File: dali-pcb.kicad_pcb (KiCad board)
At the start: 2 copper layers, 180.5 x 113 mm, 62 parts, among them J1 12-22.5V DC, J10 5V DC, J11 5V DC, J12 5V DC, J13 5V DC, J14 5V DC, J15 GND, J2 DALI BUS, J20 LOLIN-S3 (L), J21 LOLIN-S3 (R), J22 ESP32-S3-DEVKITC-1 (L), J23 ESP32-S3-DEVKITC-1 (R), J24 LOLIN-S3-MINI (L), J25 LOLIN-S3-MINI (R), J26 LOLIN-S2-MINI (L), J27 LOLIN-S2-MINI (R), J3 DALI BUS, J30 FTDI-MCU, J31 UART-DALI, J4 DALI BUS, J40 A10-0, J41 A5-0, J42 A5-5, J43 A2-0, J44 A2-2, J45 A2-4, J46 A2-6, J47 A2-8, J50 D8-11, J51 D4-11, J52 D4-16, J53 D2-11, J54 D2-13, J55 D2-16, J56 D2-18, J60 D1-11, J61 D1-12, J62 D1-13, J63 D1-14, Q1 PZT2222A, Q2 MMBT2222A, U1 TCLT1000, U2 TCLT1000

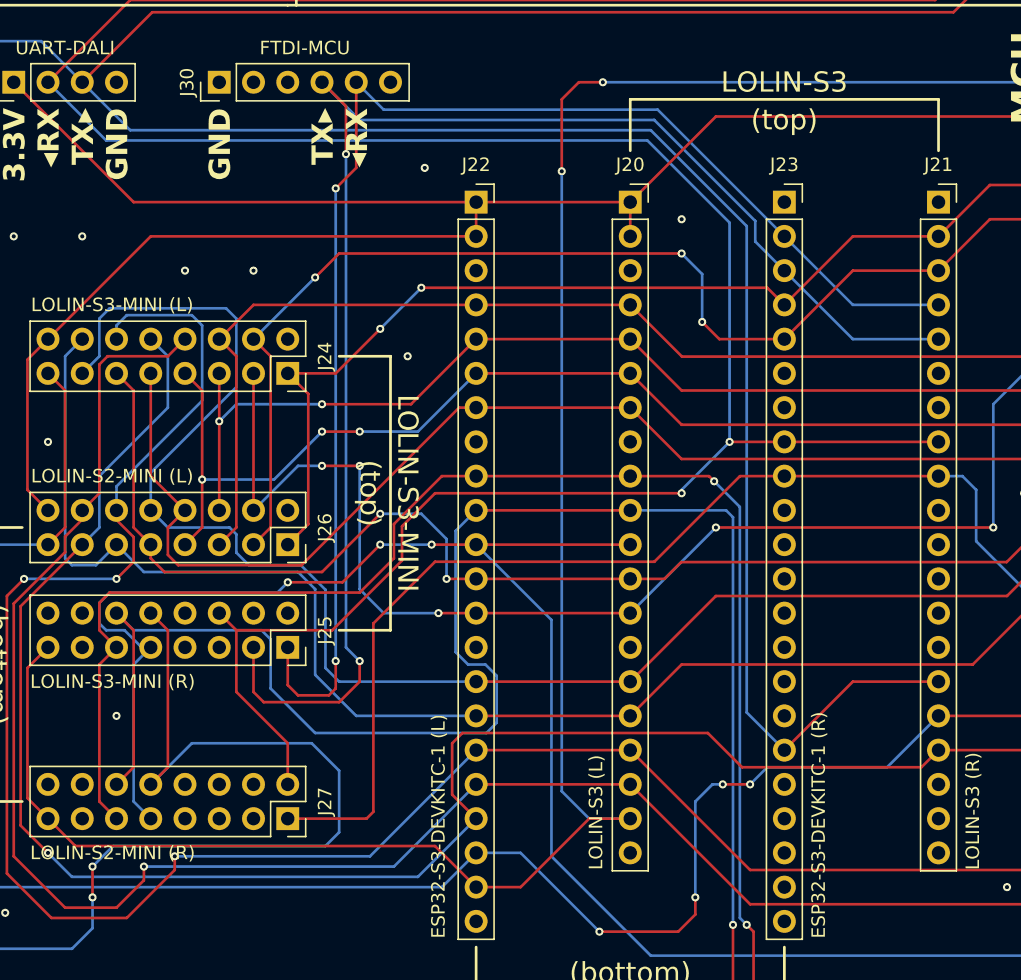
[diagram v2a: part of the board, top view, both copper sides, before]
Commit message: Fix ESP32-S3-DEVKITC-1 bottom right pins
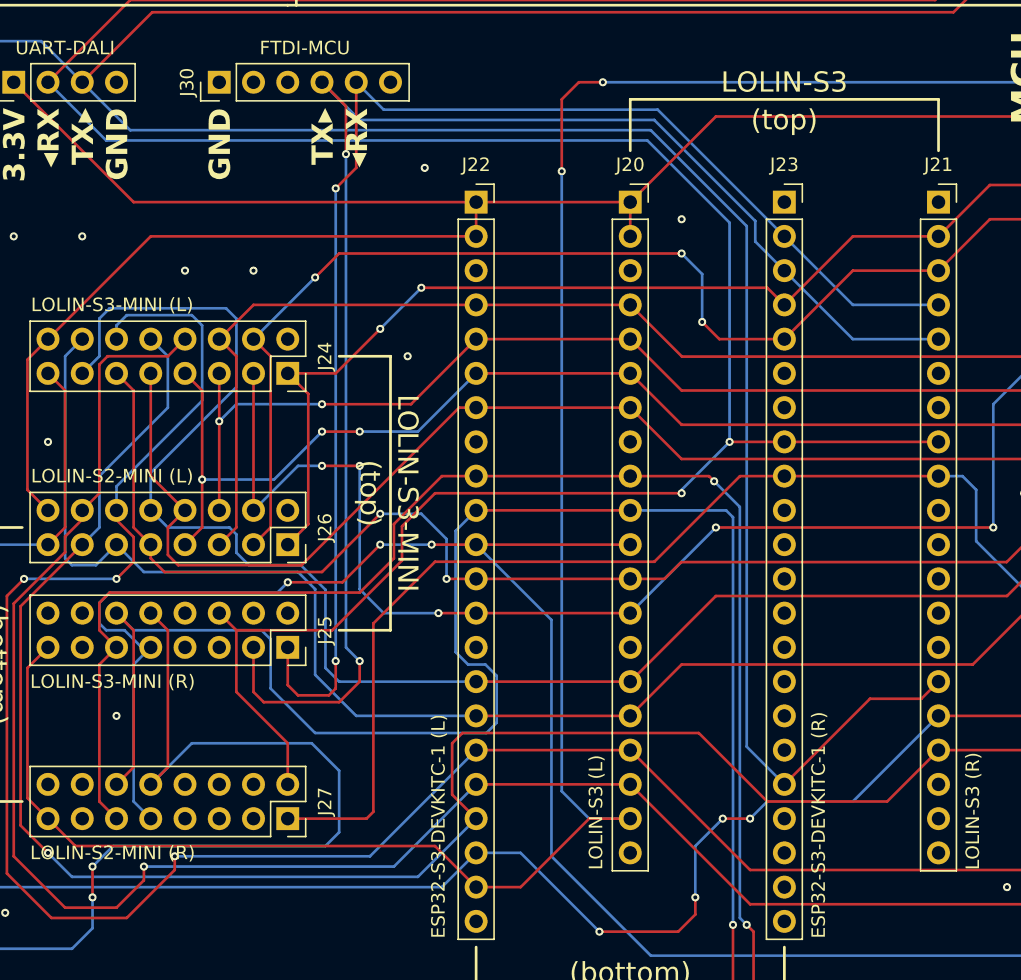
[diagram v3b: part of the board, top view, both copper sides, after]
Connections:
- J23 pad 17: /DALI/DALI_TX -> unconnected-(J23-Pin_17-Pad17)
- J23 pad 18: unconnected-(J23-Pin_18-Pad18) -> /DALI/DALI_TX
- J23 pad 20: GND -> unconnected-(J23-Pin_20-Pad20)
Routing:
- net /DALI/DALI_TX: track 328.7 -> 332.3 mm
- net /IO/IO_D13: track 339.9 -> 342.0 mm
- net /IO/IO_D14: track 306.6 -> 304.6 mm
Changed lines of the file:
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@@
 	(net 45 "unconnected-(J22-Pin_3-Pad3)")
 	(net 46 "unconnected-(J23-Pin_13-Pad13)")
-	(net 47 "unconnected-(J23-Pin_18-Pad18)")
+	(net 47 "unconnected-(J23-Pin_17-Pad17)")
 	(net 48 "unconnected-(J23-Pin_19-Pad19)")
 	(net 49 "unconnected-(J23-Pin_12-Pad12)")
@@
 	(net 80 "unconnected-(J27-Pin_8-Pad8)")
 	(net 81 "unconnected-(J27-Pin_6-Pad6)")
+	(net 82 "unconnected-(J23-Pin_20-Pad20)")
 	(footprint "Package_TO_SOT_SMD:SOT-23"
 		(placed yes)
@@
 			(layers "*.Cu" "*.Mask")
 			(remove_unused_layers no)
-			(net 33 "/DALI/DALI_TX")
+			(net 47 "unconnected-(J23-Pin_17-Pad17)")
 			(pinfunction "Pin_17")
-			(pintype "passive")
+			(pintype "passive+no_connect")
 		)
 		(pad "18" thru_hole circle
@@
 			(layers "*.Cu" "*.Mask")
 			(remove_unused_layers no)
-			(net 47 "unconnected-(J23-Pin_18-Pad18)")
+			(net 33 "/DALI/DALI_TX")
 			(pinfunction "Pin_18")
-			(pintype "passive+no_connect")
+			(pintype "passive")
 		)
 		(pad "19" thru_hole circle
@@
 			(layers "*.Cu" "*.Mask")
 			(remove_unused_layers no)
-			(net 9 "GND")
+			(net 82 "unconnected-(J23-Pin_20-Pad20)")
 			(pinfunction "Pin_20")
-			(pintype "passive")
+			(pintype "passive+no_connect")
 		)
 		(pad "21" thru_hole circle
@@
 	)
 	(segment
-		(start 97.63281 50.68719)
-		(end 38.21281 50.68719)
+		(start 91.44 101.6)
+		(end 95.25 101.6)
 		(width 0.2)
 		(layer "F.Cu")
@@
 	)
 	(segment
-		(start 85.09 105.41)
-		(end 90.17 100.33)
+		(start 85.09 107.95)
+		(end 91.44 101.6)
+		(width 0.2)
+		(layer "F.Cu")
+		(net 33)
+	)
+	(segment
+		(start 97.63281 50.68719)
+		(end 38.21281 50.68719)
 		(width 0.2)
 		(layer "F.Cu")
@@
 	)
 	(segment
+		(start 95.25 101.6)
+		(end 96.52 100.33)
+		(width 0.2)
+		(layer "F.Cu")
+		(net 33)
+	)
+	(segment
 		(start 39.37 96.52)
 		(end 39.37 106.68)
@@
 	)
 	(segment
-		(start 90.17 100.33)
-		(end 96.52 100.33)
-		(width 0.2)
-		(layer "F.Cu")
-		(net 33)
-	)
-	(segment
 		(start 38.21281 50.68719)
 		(end 33.02 55.88)
@@
 	)
 	(segment
+		(start 75.184 59.436)
+		(end 82.296 66.548)
+		(width 0.2)
+		(layer "B.Cu")
+		(net 33)
+	)
+	(segment
 		(start 50.038 104.902)
 		(end 52.07 106.934)
@@
 	)
 	(segment
-		(start 82.296 102.616)
-		(end 82.296 66.548)
-		(width 0.2)
-		(layer "B.Cu")
-		(net 33)
-	)
-	(segment
-		(start 75.184 59.436)
-		(end 36.576 59.436)
-		(width 0.2)
-		(layer "B.Cu")
-		(net 33)
-	)
-	(segment
-		(start 85.09 105.41)
-		(end 82.296 102.616)
-		(width 0.2)
-		(layer "B.Cu")
-		(net 33)
-	)
-	(segment
 		(start 33.782 118.618)
 		(end 32.258 120.142)
@@
 	)
 	(segment
+		(start 36.576 59.436)
+		(end 75.184 59.436)
+		(width 0.2)
+		(layer "B.Cu")
+		(net 33)
+	)
+	(segment
 		(start 51.054 112.522)
 		(end 52.07 111.506)
@@
 	)
 	(segment
-		(start 36.576 59.436)
-		(end 33.02 55.88)
+		(start 82.296 105.156)
+		(end 85.09 107.95)
 		(width 0.2)
 		(layer "B.Cu")
@@
 	)
 	(segment
-		(start 82.296 66.548)
-		(end 75.184 59.436)
+		(start 33.02 55.88)
+		(end 36.576 59.436)
 		(width 0.2)
 		(layer "B.Cu")
@@
 	)
 	(segment
+		(start 82.296 66.548)
+		(end 82.296 105.156)
+		(width 0.2)
+		(layer "B.Cu")
+		(net 33)
+	)
+	(segment
 		(start 41.148 104.902)
 		(end 50.038 104.902)
@@
 	)
 	(segment
+		(start 60.452 108.712)
+		(end 62.23 110.49)
+		(width 0.2)
+		(layer "F.Cu")
+		(net 38)
+	)
+	(segment
 		(start 28.448 94.742)
 		(end 33.02 90.17)
@@
 	)
 	(segment
-		(start 61.214 104.14)
-		(end 60.452 104.902)
+		(start 92.71 109.22)
+		(end 83.82 109.22)
 		(width 0.2)
 		(layer "F.Cu")
@@
 	)
 	(segment
-		(start 95.25 106.68)
-		(end 81.95424 106.68)
+		(start 61.214 104.14)
+		(end 60.452 104.902)
 		(width 0.2)
 		(layer "F.Cu")
@@
 	)
 	(segment
+		(start 96.52 105.41)
+		(end 92.71 109.22)
+		(width 0.2)
+		(layer "F.Cu")
+		(net 38)
+	)
+	(segment
 		(start 184.912 102.108)
 		(end 184.912 90.424)
@@
 	)
 	(segment
-		(start 182.88 104.14)
-		(end 181.61 105.41)
+		(start 60.452 104.902)
+		(end 60.452 108.712)
 		(width 0.2)
 		(layer "F.Cu")
@@
 	)
 	(segment
-		(start 60.452 104.902)
-		(end 60.452 108.712)
+		(start 182.88 104.14)
+		(end 181.61 105.41)
 		(width 0.2)
 		(layer "F.Cu")
@@
 	)
 	(segment
-		(start 96.52 105.41)
-		(end 95.25 106.68)
+		(start 78.74 104.14)
+		(end 61.214 104.14)
 		(width 0.2)
 		(layer "F.Cu")
@@
 	)
 	(segment
-		(start 60.452 108.712)
-		(end 62.23 110.49)
-		(width 0.2)
-		(layer "F.Cu")
-		(net 38)
-	)
-	(segment
-		(start 81.95424 106.68)
-		(end 79.41424 104.14)
+		(start 83.82 109.22)
+		(end 78.74 104.14)
 		(width 0.2)
 		(layer "F.Cu")
@@
 		(net 38)
 	)
-	(segment
-		(start 79.41424 104.14)
-		(end 61.214 104.14)
-		(width 0.2)
-		(layer "F.Cu")
-		(net 38)
-	)
 	(via
 		(at 30.48 113.03)
@@
 	)
 	(segment
-		(start 82.55 107.95)
-		(end 80.518 107.95)
+		(start 80.518 110.49)
+		(end 82.55 110.49)
 		(width 0.2)
 		(layer "F.Cu")
@@
 	)
 	(via
-		(at 80.518 107.95)
+		(at 80.518 110.49)
 		(size 0.6)
 		(drill 0.3)
@@
 	)
 	(via
-		(at 82.55 107.95)
+		(at 82.55 110.49)
 		(size 0.6)
 		(drill 0.3)
@@
 	)
 	(segment
+		(start 90.17 109.22)
+		(end 96.52 102.87)
+		(width 0.2)
+		(layer "B.Cu")
+		(net 39)
+	)
+	(segment
 		(start 62.23 113.03)
 		(end 59.69 115.57)
@@
 	)
 	(segment
-		(start 92.71 106.68)
-		(end 96.52 102.87)
+		(start 83.82 109.22)
+		(end 90.17 109.22)
 		(width 0.2)
 		(layer "B.Cu")
@@
 	)
 	(segment
-		(start 79.756 107.95)
-		(end 78.486 109.22)
+		(start 78.486 112.522)
+		(end 78.486 116.332)
 		(width 0.2)
 		(layer "B.Cu")
@@
 	)
 	(segment
+		(start 82.55 110.49)
+		(end 83.82 109.22)
+		(width 0.2)
+		(layer "B.Cu")
+		(net 39)
+	)
+	(segment
 		(start 25.4 114.554)
 		(end 25.4 91.44)
@@
 	)
 	(segment
-		(start 83.82 106.68)
-		(end 92.71 106.68)
+		(start 80.518 110.49)
+		(end 78.486 112.522)
 		(width 0.2)
 		(layer "B.Cu")
@@
 	)
 	(segment
-		(start 78.486 109.22)
-		(end 78.486 116.332)
-		(width 0.2)
-		(layer "B.Cu")
-		(net 39)
-	)
-	(segment
 		(start 59.69 115.57)
 		(end 26.416 115.57)
@@
 	)
 	(segment
-		(start 82.55 107.95)
-		(end 83.82 106.68)
-		(width 0.2)
-		(layer "B.Cu")
-		(net 39)
-	)
-	(segment
 		(start 134.366 81.534)
 		(end 120.904 94.996)
@@
 		(width 0.2)
 		(layer "B.Cu")
-		(net 39)
-	)
-	(segment
-		(start 80.518 107.95)
-		(end 79.756 107.95)
-		(width 0.2)
-		(layer "B.Cu")

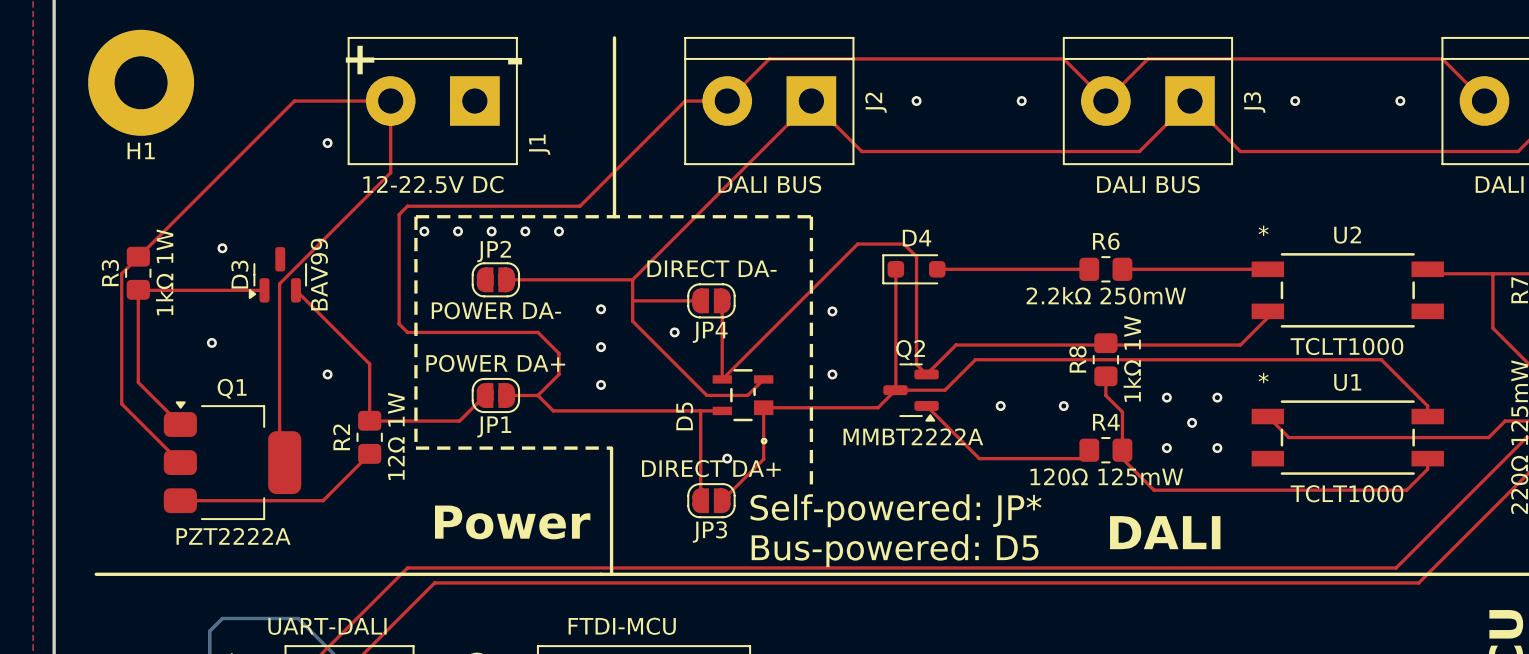
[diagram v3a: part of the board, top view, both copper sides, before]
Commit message: Check and list components
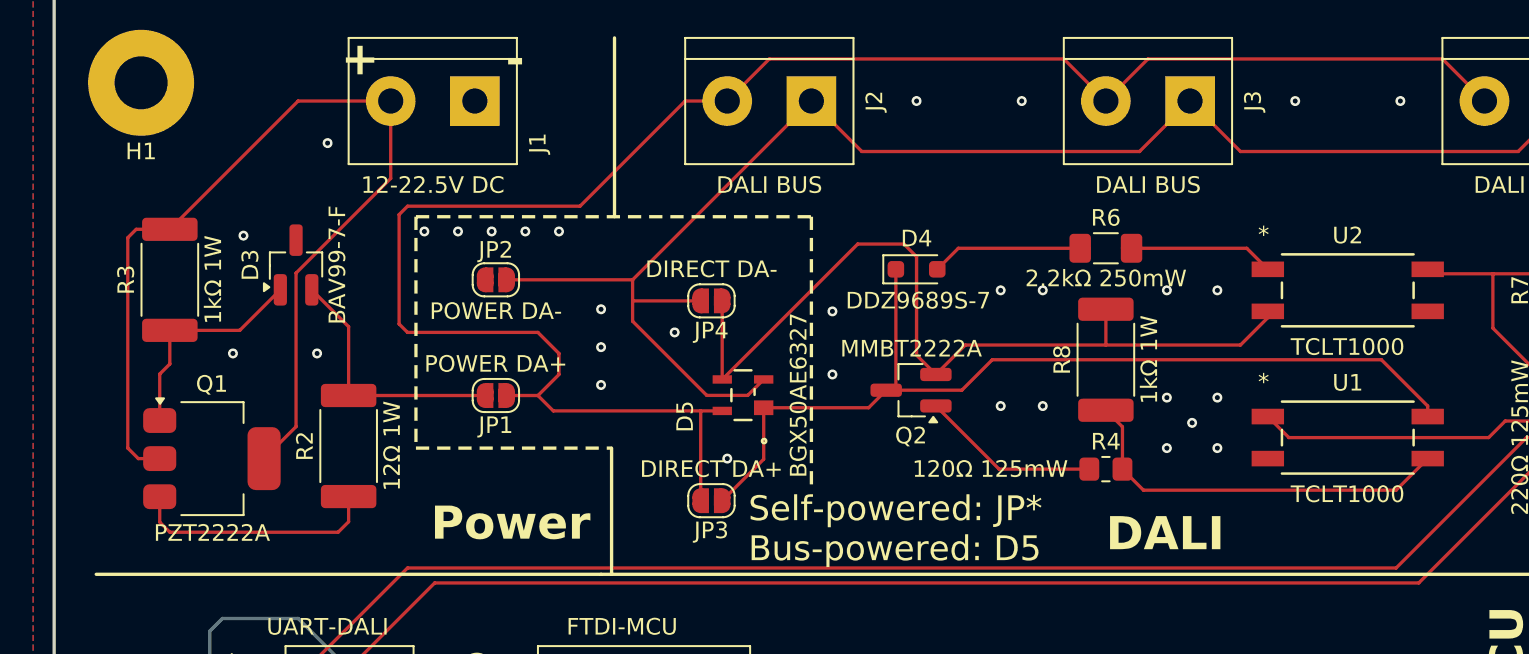
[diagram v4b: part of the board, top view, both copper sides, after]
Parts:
- D3: value BAV99 -> BAV99-7-F; footprint Package_TO_SOT_SMD:SOT-23 -> Package_TO_SOT_SMD:SOT-23_Handsoldering
- D4: value D_Zener -> DDZ9689S-7
- D5: value D_Bridge_+A-A -> BGX50AE6327
- Q2: footprint Package_TO_SOT_SMD:SOT-23 -> Package_TO_SOT_SMD:SOT-23_Handsoldering
- R2, R3, R8: footprint Resistor_SMD:R_0805_2012Metric_Pad1.20x1.40mm_HandSolder -> Resistor_SMD:R_2512_6332Metric_Pad1.40x3.35mm_HandSolder
- R6: footprint Resistor_SMD:R_0805_2012Metric_Pad1.20x1.40mm_HandSolder -> Resistor_SMD:R_1206_3216Metric_Pad1.30x1.75mm_HandSolder
- moved R3 1.95 mm to (22.2, 32.4)
- moved R2 1.37 mm to (33.0, 42.4)
- moved R6 1.27 mm to (78.7, 30.5)
- moved Q1 1.27 mm to (24.8, 43.2)
- moved R4 1.14 mm to (78.7, 43.8)
- moved D3 1.12 mm to (29.8, 31.5)
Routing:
- net Net-(Q1-B): track 16.8 -> 13.4 mm
- net Net-(Q1-E): track 12.6 -> 15.0 mm
- net Net-(D5--): track 49.9 -> 51.8 mm
- net /Power/DA+: track 17.3 -> 15.5 mm
- net Net-(R4-Pad2): track 25.3 -> 23.7 mm
- net +12-22.5V DC: track 57.7 -> 58.9 mm
- net Net-(D4-A): track 9.18 -> 9.79 mm
- net Net-(R6-Pad2): track 8.78 -> 9.39 mm
- net Net-(D4-K): track 57.0 -> 56.4 mm
- net Net-(Q2-B): track 11.4 -> 10.8 mm
- net GND: vias 49 -> 53
